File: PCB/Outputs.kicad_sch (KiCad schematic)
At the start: 2 parts, among them J3 SSD1306, U2 Music Maker FeatherWing

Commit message: Restarted the schematic
It was getting way to full.
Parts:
- removed J3: SSD1306, CustomFootprints:SSD1306_128x64, symbol Connector_Generic:Conn_01x04
- removed U2: Music Maker FeatherWing, CustomFootprints:Music_Maker_Feather_Wing, symbol CustomSymbols:Music_Maker_FeatherWing
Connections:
- no-connect marks 14 -> 0
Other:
- company: (none) -> Joshua E
- title: (none) -> Music Player

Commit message: Finished the schematic.
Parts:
- added C15: 100n, Capacitor_SMD:C_0201_0603Metric, symbol Device:C
- added D5: ERROR, LED_SMD:LED_0201_0603Metric, symbol Device:LED
- added D6: PAUSE, LED_SMD:LED_0201_0603Metric, symbol Device:LED
- added D7: PLAY, LED_SMD:LED_0201_0603Metric, symbol Device:LED
- added J3: SSD1306D, CustomFootprints:SSD1306_128x64, symbol Connector_Generic:Conn_01x04
- added J5: Conn_01x04_Socket, Connector_PinSocket_2.54mm:PinSocket_1x04_P2.54mm_Vertical, symbol Connector:Conn_01x04_Socket
- added J6: Conn_01x16_Socket, Connector_PinSocket_2.54mm:PinSocket_1x16_P2.54mm_Vertical, symbol Connector:Conn_01x16_Socket
- added J7: Conn_01x12_Socket, Connector_PinSocket_2.54mm:PinSocket_1x12_P2.54mm_Vertical, symbol Connector:Conn_01x12_Socket
- added R18, R19: 470, Resistor_SMD:R_0201_0603Metric, symbol Device:R
- added R20: 36.1, Resistor_SMD:R_0201_0603Metric, symbol Device:R
- added U5: Music Maker FeatherWing, CustomFootprints:Music_Maker_Feather_Wing, symbol CustomSymbols:Music_Maker_FeatherWing
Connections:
- new net: D7.1 (K), R20.1
- new net: D6.1 (K), R19.1
- new net: D5.1 (K), R18.1
- new net +3V3: C15.2, J3.2 (Pin_2), J5.2 (Pin_2), J6.2 (Pin_2), U5.2 (3V3)
- new net +5V: J7.1 (Pin_1), U5.28 (VBAT)
- new net DREQ: J7.8 (Pin_8), U5.21 (DREQ)
- new net GND: C15.1, J3.1 (Pin_1), J5.1 (Pin_1), J6.3 (Pin_3), R18.2, R19.2, R20.2, U5.4 (GND)
- new net LED_ERROR: D5.2 (A)
- new net LED_PAUSED: D6.2 (A)
- new net LED_PLAYING: D7.2 (A)
- new net MISO: J6.11 (Pin_11), U5.13 (MISO)
- new net MOSI: J6.12 (Pin_12), U5.12 (MOSI)
- new net RESET: J6.1 (Pin_1), U5.1 (RESET)
- new net SCK: J6.13 (Pin_13), U5.11 (SCK)
- new net SCL: J3.3 (Pin_3), J5.3 (Pin_3), J7.11 (Pin_11), U5.18 (SCL)
- new net SDA: J3.4 (Pin_4), J5.4 (Pin_4), J7.12 (Pin_12), U5.17 (SDA)
- new net SD_CS: J7.10 (Pin_10), U5.19 (SD_CS)
- new net VBUS: J7.3 (Pin_3), U5.26 (USB)
- new net XD_CS: J7.7 (Pin_7), U5.22 (XD_CS)
- new net X_CS: J7.9 (Pin_9), U5.20 (X_CS)
- no-connect marks 0 -> 28

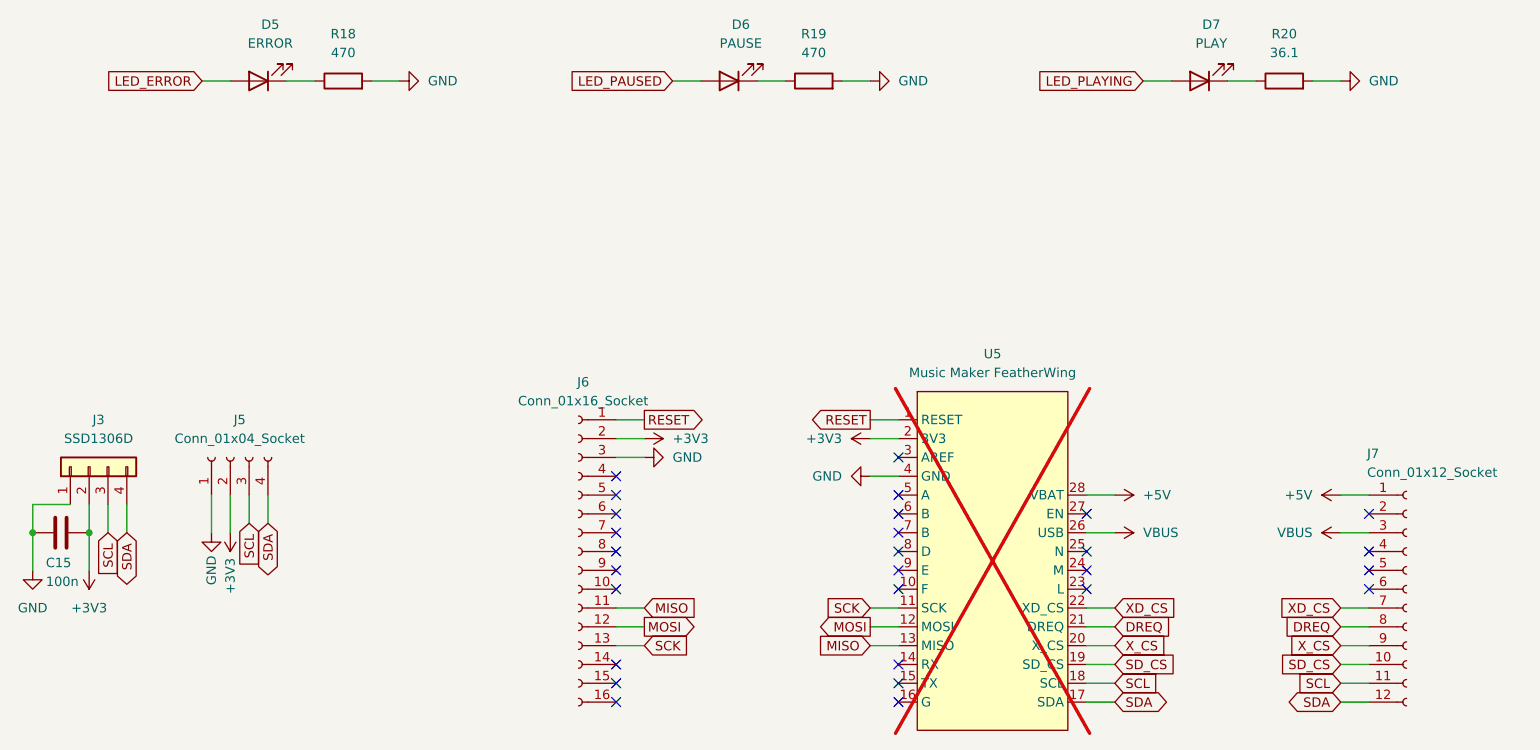
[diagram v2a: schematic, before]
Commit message: fixed schematic errors
Accidentally set all SMD 0603 to SMD 0603 metric
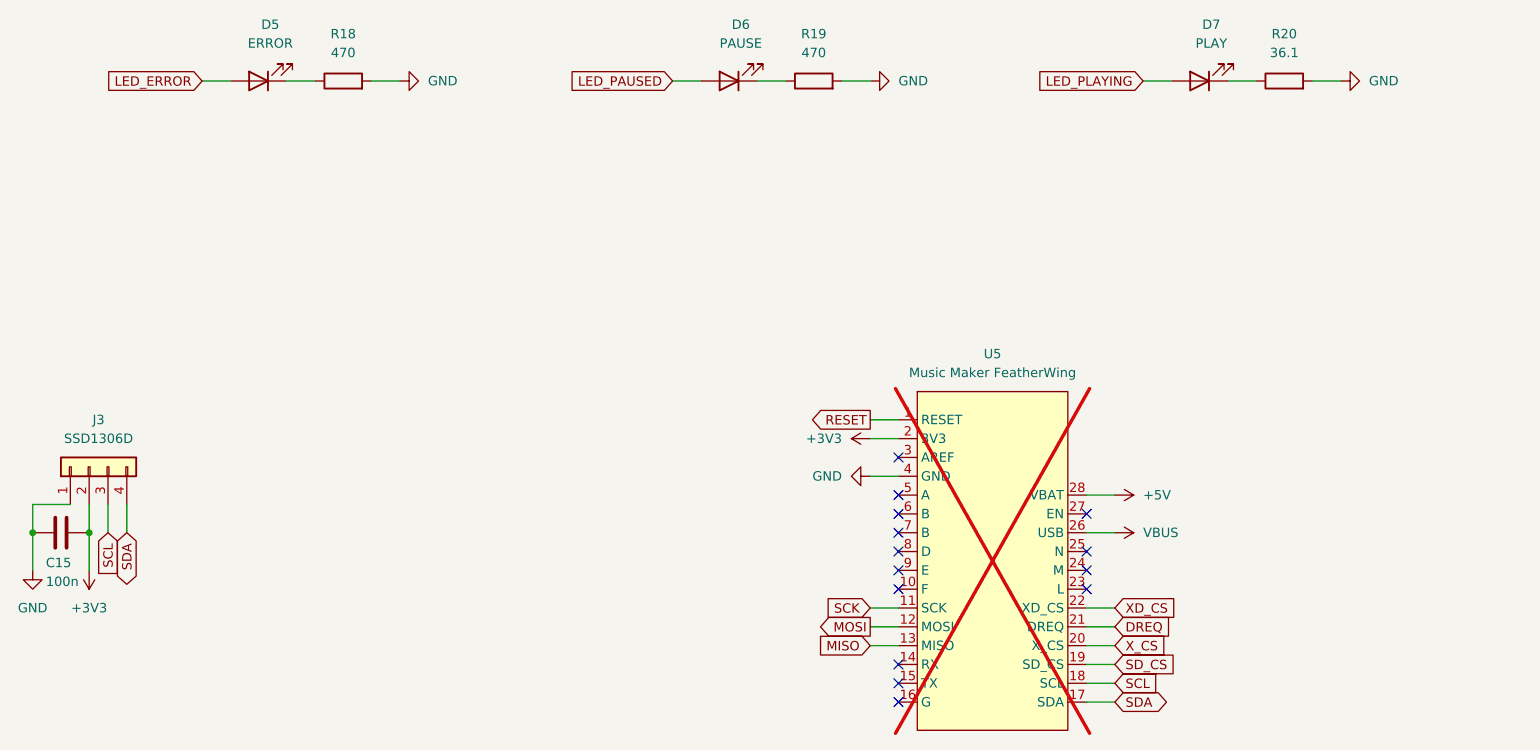
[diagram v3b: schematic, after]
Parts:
- removed J5: Conn_01x04_Socket, Connector_PinSocket_2.54mm:PinSocket_1x04_P2.54mm_Vertical, symbol Connector:Conn_01x04_Socket
- removed J6: Conn_01x16_Socket, Connector_PinSocket_2.54mm:PinSocket_1x16_P2.54mm_Vertical, symbol Connector:Conn_01x16_Socket
- removed J7: Conn_01x12_Socket, Connector_PinSocket_2.54mm:PinSocket_1x12_P2.54mm_Vertical, symbol Connector:Conn_01x12_Socket
- C15: footprint Capacitor_SMD:C_0201_0603Metric -> Capacitor_SMD:C_0603_1608Metric
- D5, D6, D7: footprint LED_SMD:LED_0201_0603Metric -> LED_SMD:LED_0603_1608Metric
- J3: footprint CustomFootprints:SSD1306_128x64 -> Connector_PinSocket_2.54mm:PinSocket_1x04_P2.54mm_Vertical
- R18, R19, R20: footprint Resistor_SMD:R_0201_0603Metric -> Resistor_SMD:R_0603_1608Metric
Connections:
- no-connect marks 28 -> 14

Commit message: Finished making a PCB for it
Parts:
- J3: LCSC C2905421 -> C2718488
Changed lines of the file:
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@@
 			)
 		)
-		(property "LCSC" "C2905421"
+		(property "LCSC" "C2718488"
 			(at 43.18 90.17 90)
 			(effects
